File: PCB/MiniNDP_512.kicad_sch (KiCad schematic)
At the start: 20 parts, among them J1 Conn_02x20_Odd_Even, U1 HC161, U2 HC161, U3 HC161, U4 HC138, U5 HC374, U6 AS6C4008, U7 1G32, U8 1G79

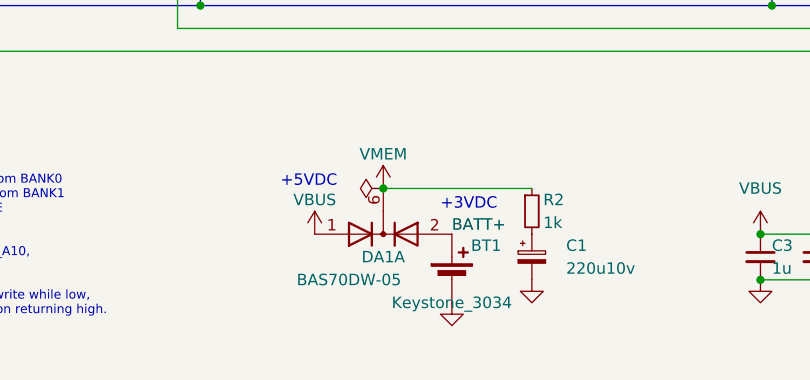
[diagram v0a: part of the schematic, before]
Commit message: Redraw 1M for SOIC-24 FCT821, 2mm corners, remove corner holes, update cover
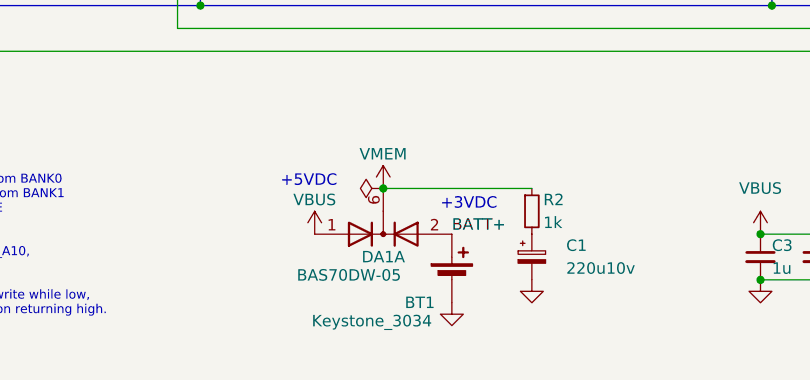
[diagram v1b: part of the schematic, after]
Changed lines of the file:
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@@
 		(dnp no)
 		(property "Reference" "BT1"
-			(at 104.14 181.61 0)
+			(at 96.774 187.96 0)
 			(effects
 				(font
@@
 		)
 		(property "Value" "Keystone_3034"
-			(at 100.33 187.96 0)
+			(at 91.44 189.992 0)
 			(effects
 				(font
@@
 		)
 		(property "Value" "BAS70DW-05"
-			(at 88.9 185.42 0)
-			(effects
-				(font
+			(at 88.9 184.912 0)
+			(effects
+				(font

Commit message: 1M_B & 512_B
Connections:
- net BATT+ renamed +BATT
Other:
- note added: "/----- BUS -----\ (A) ~{YO} A8 A9 A10 -> ~{BLOCK} ~{BYTE} L X X X X X X X H X X X X X X X L X X X X H L H L L -> L H Select BLOCK # from BANK0 H L H L H -> L H Select BLOCK # from BANK1 H L H H X -> H L READ/WRITE BYTE Each ~{BLOCK} pulse low: sets A0-A9 to 0, sets A10-A18 from AD0-AD7 & BUS_A10, then holds A10-A18 latched while high. Each ~{BYTE} pulse low: enables SRAM for read or write while l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"
- note added: "3V"
- note added: "5V"
- note added: "BUS_A11"
- note added: "BUS_A12"
- note added: "BUS_A13"
- note added: "BUS_A14"
- note added: "BUS_A15"
- note added: "CR2032"
- note added: "For 512k: Populate U8 with 1G79 or 1G80. Keep JP1 Open. Populate U6 with AS6C4008. For 256k or 128k: Don't populate U8. Bridge JP1. Populate U6 with AS6C2008A or AS6C1008."
- note removed: "+3VDC"
- note removed: "/----- BUS -----\ (A) ~{YO} A8 A9 A10 -> ~{BLOCK} ~{BYTE} L X X X X X X X H X X X X X X X L X X X X H L H L L -> L H Select BLOCK # from BANK0 H L H L H -> L H Select BLOCK # from BANK1 H L H H X -> H L READ/WRITE BYTE Each ~{BLOCK} pulse low: sets A0-A9 to 0, sets A10-A17 from AD0-AD7, sets A18 from BUS_A10, then holds A10-A18 latched while high. Each ~{BYTE} pulse low: enables SRAM for read or 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"
- note removed: "A11"
- note removed: "A12"
- note removed: "A13"
- note removed: "A14"
- note removed: "A15"
- note removed: "BANK SELECT"
- note removed: "For 512k: Populate U8 with 1G79 or 1G80. Keep JP1 Open. Populate U6 with AS6C4008. For 256k or 128k: Don't populate U8. Close JP1. Populate U6 with AS6C2008A or AS6C1008."
- moved on the sheet: BT1, C1, C3, C4, C5, C6, DA1A, DA1B, J1, R1, R2, U1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

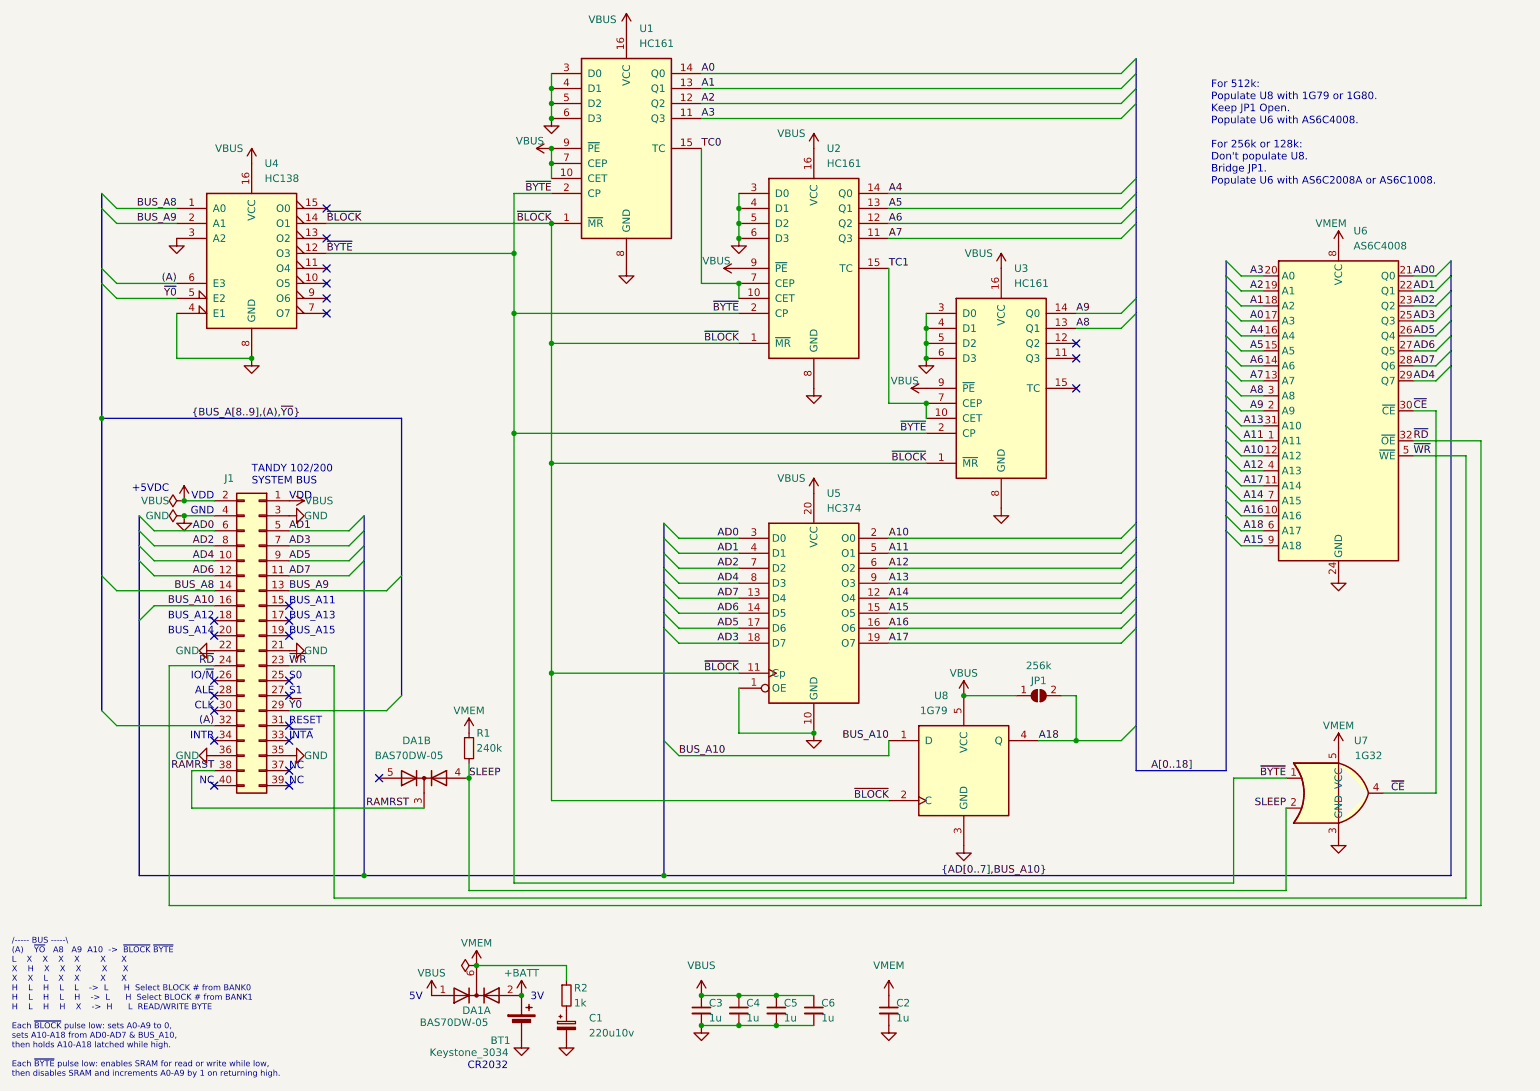
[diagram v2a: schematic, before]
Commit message: fix 128k compatibility, AD7->A17->pin9
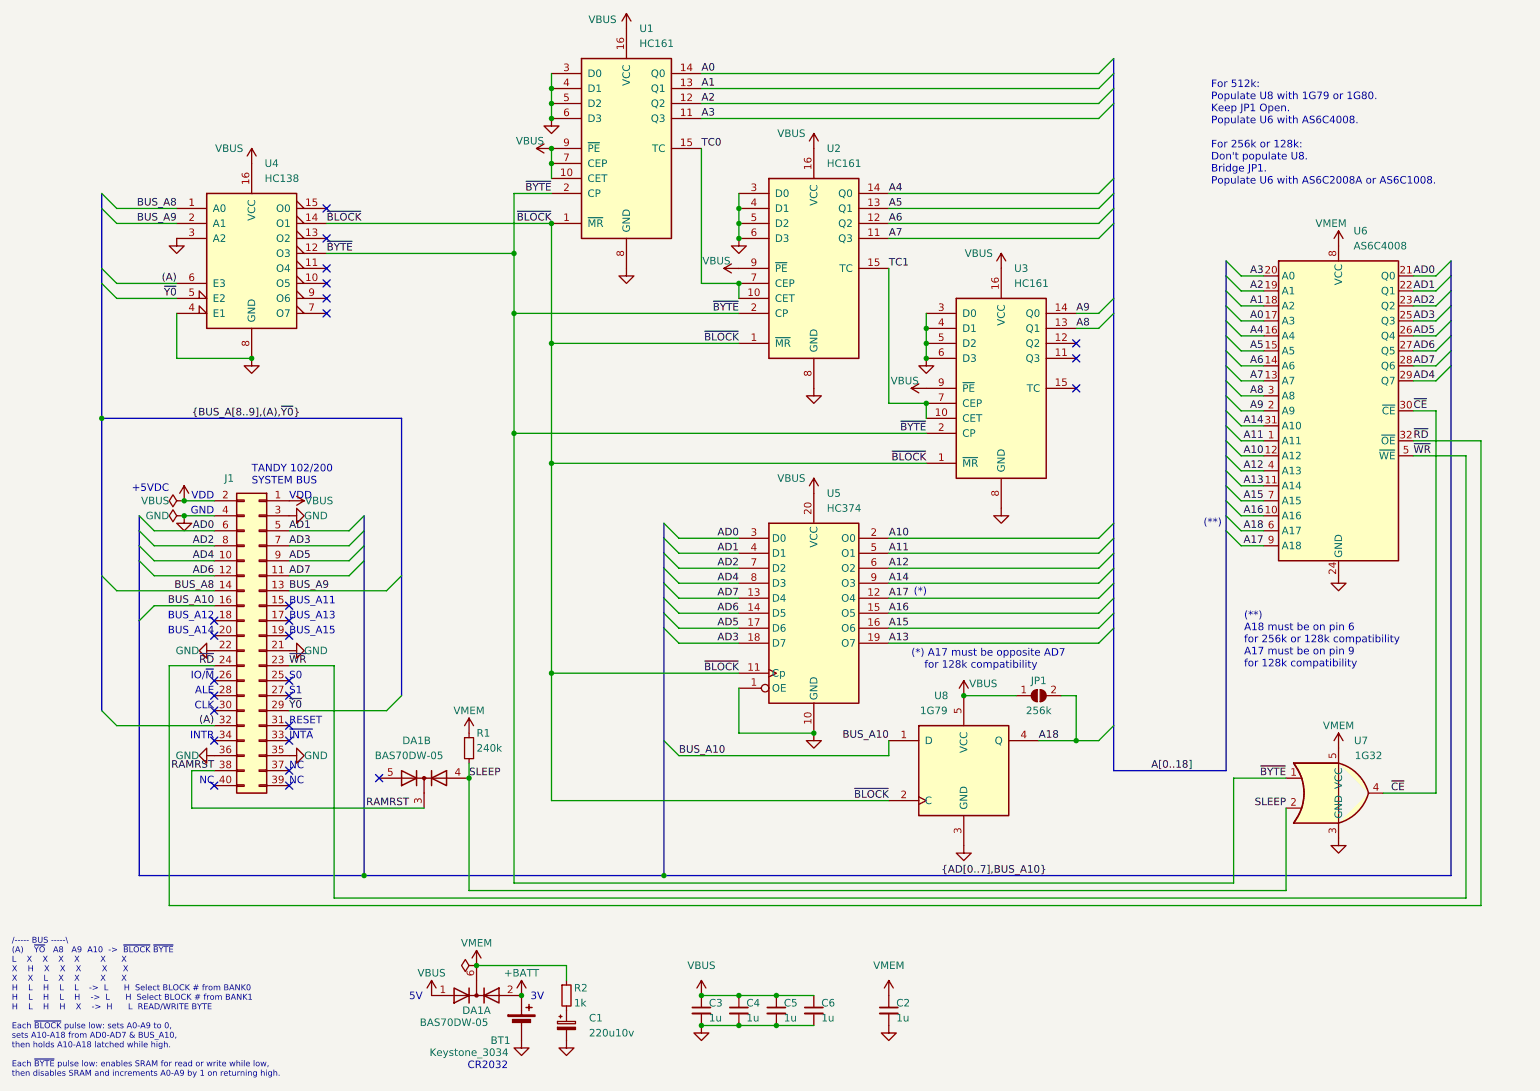
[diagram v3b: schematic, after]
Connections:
- net A13: now also U5.19 (O7), U6.11 (A14); no longer U5.9 (O3), U6.31 (A10)
- net A14: now also U5.9 (O3), U6.31 (A10); no longer U5.12 (O4), U6.7 (A15)
- net A15: now also U5.16 (O6), U6.7 (A15); no longer U5.15 (O5), U6.9 (A18)
- net A16: now also U5.15 (O5); no longer U5.16 (O6)
- net A17: now also U5.12 (O4), U6.9 (A18); no longer U5.19 (O7), U6.11 (A14)
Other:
- note added: "(*)"
- note added: "(*) A17 must be opposite AD7 for 128k compatibility"
- note added: "(**)"
- note added: "(**) A18 must be on pin 6 for 256k or 128k compatibility A17 must be on pin 9 for 128k compatibility"

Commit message: Add pullup on /WR. Tighter cover fit.
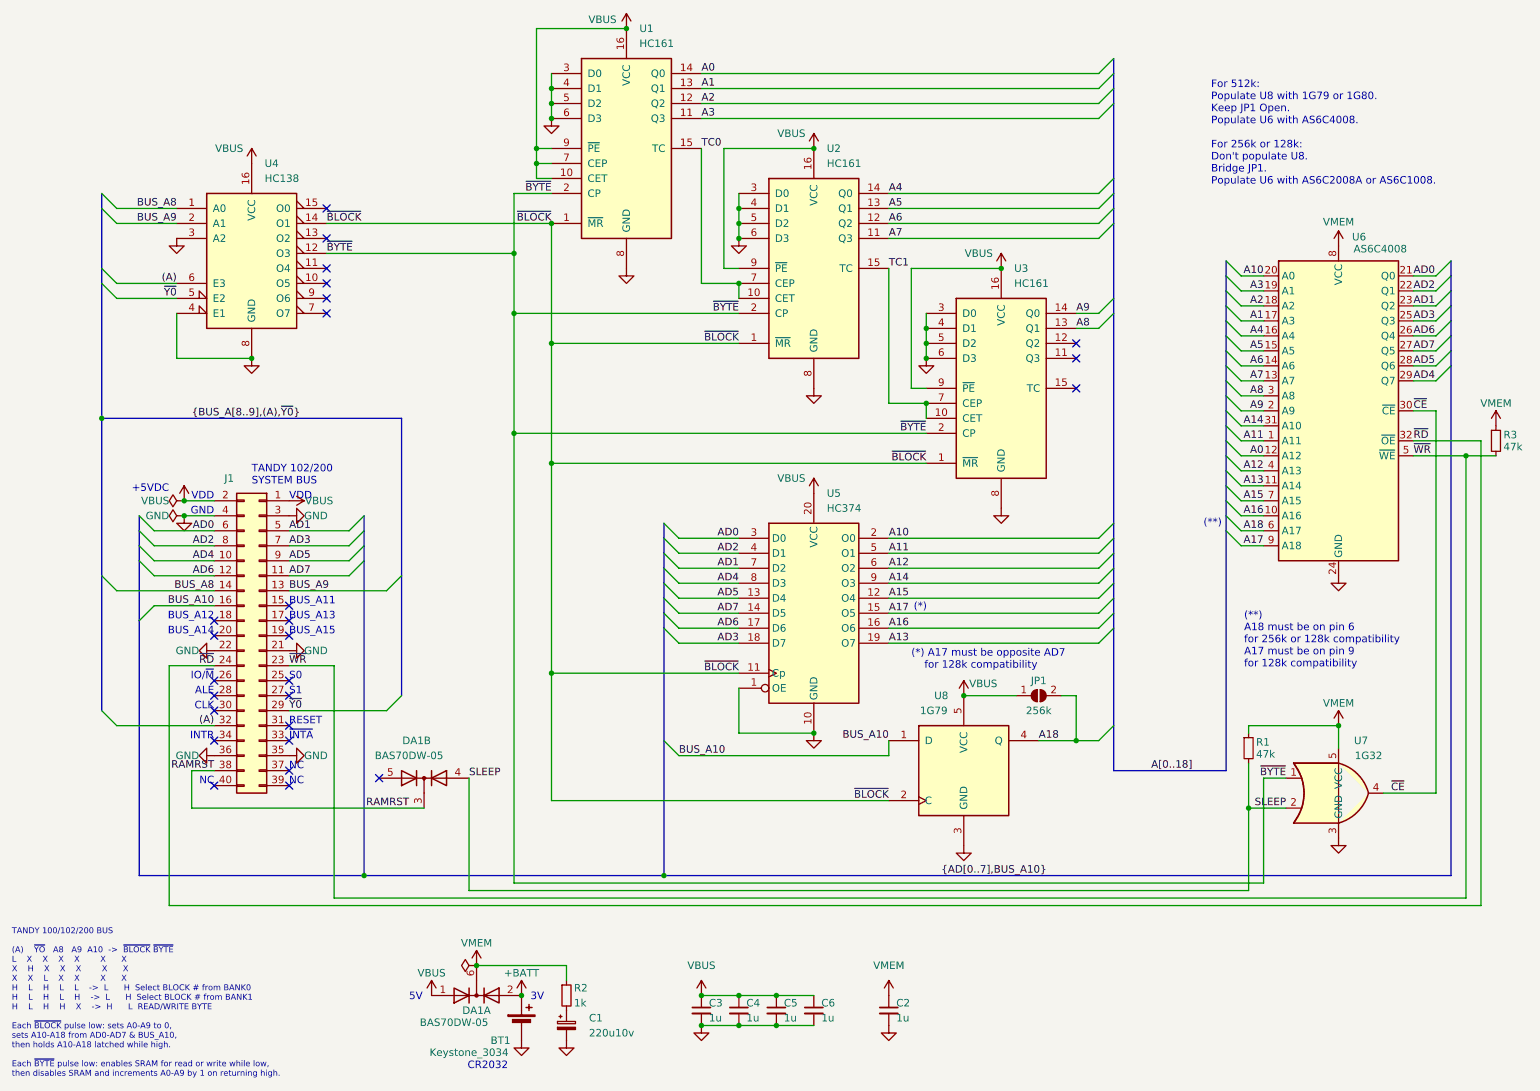
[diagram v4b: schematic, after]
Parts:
- added R3: 47k, 000_LOCAL:R_0805, symbol 000_LOCAL:R
- R1: value 240k -> 47k
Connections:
- net A0: now also U6.12 (A12); no longer U6.17 (A3)
- net A1: now also U6.17 (A3); no longer U6.18 (A2)
- net A10: now also U6.20 (A0); no longer U6.12 (A12)
- net A15: now also U5.12 (O4); no longer U5.16 (O6)
- net A16: now also U5.16 (O6); no longer U5.15 (O5)
- net A17: now also U5.15 (O5); no longer U5.12 (O4)
- net A2: now also U6.18 (A2); no longer U6.19 (A1)
- net A3: now also U6.19 (A1); no longer U6.20 (A0)
- net AD1: now also U5.7 (D2), U6.23 (Q2); no longer U5.4 (D1), U6.22 (Q1)
- net AD2: now also U5.4 (D1), U6.22 (Q1); no longer U5.7 (D2), U6.23 (Q2)
- net AD5: now also U5.13 (D4), U6.28 (Q6); no longer U5.17 (D6), U6.26 (Q4)
- net AD6: now also U5.17 (D6), U6.26 (Q4); no longer U5.14 (D5), U6.27 (Q5)
- net AD7: now also U5.14 (D5), U6.27 (Q5); no longer U5.13 (D4), U6.28 (Q6)
- net VMEM: now also R3.1
- net ~{WR}: now also R3.2
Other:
- note added: "TANDY 100/102/200 BUS (A) ~{YO} A8 A9 A10 -> ~{BLOCK} ~{BYTE} L X X X X X X X H X X X X X X X L X X X X H L H L L -> L H Select BLOCK # from BANK0 H L H L H -> L H Select BLOCK # from BANK1 H L H H X -> H L READ/WRITE BYTE Each ~{BLOCK} pulse low: sets A0-A9 to 0, sets A10-A18 from AD0-AD7 & BUS_A10, then holds A10-A18 latched while high. Each ~{BYTE} pulse low: enables SRAM for read or write whi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"
- note removed: "/----- BUS -----\ (A) ~{YO} A8 A9 A10 -> ~{BLOCK} ~{BYTE} L X X X X X X X H X X X X X X X L X X X X H L H L L -> L H Select BLOCK # from BANK0 H L H L H -> L H Select BLOCK # from BANK1 H L H H X -> H L READ/WRITE BYTE Each ~{BLOCK} pulse low: sets A0-A9 to 0, sets A10-A18 from AD0-AD7 & BUS_A10, then holds A10-A18 latched while high. Each ~{BYTE} pulse low: enables SRAM for read or write while l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"
- moved on the sheet: R1
